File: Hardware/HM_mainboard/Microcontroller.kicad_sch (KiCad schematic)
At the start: 13 parts, among them J7 USB_C_Receptacle_USB2.0, U5 ESP32-S3-WROOM-1, Y1 32.768 kHz

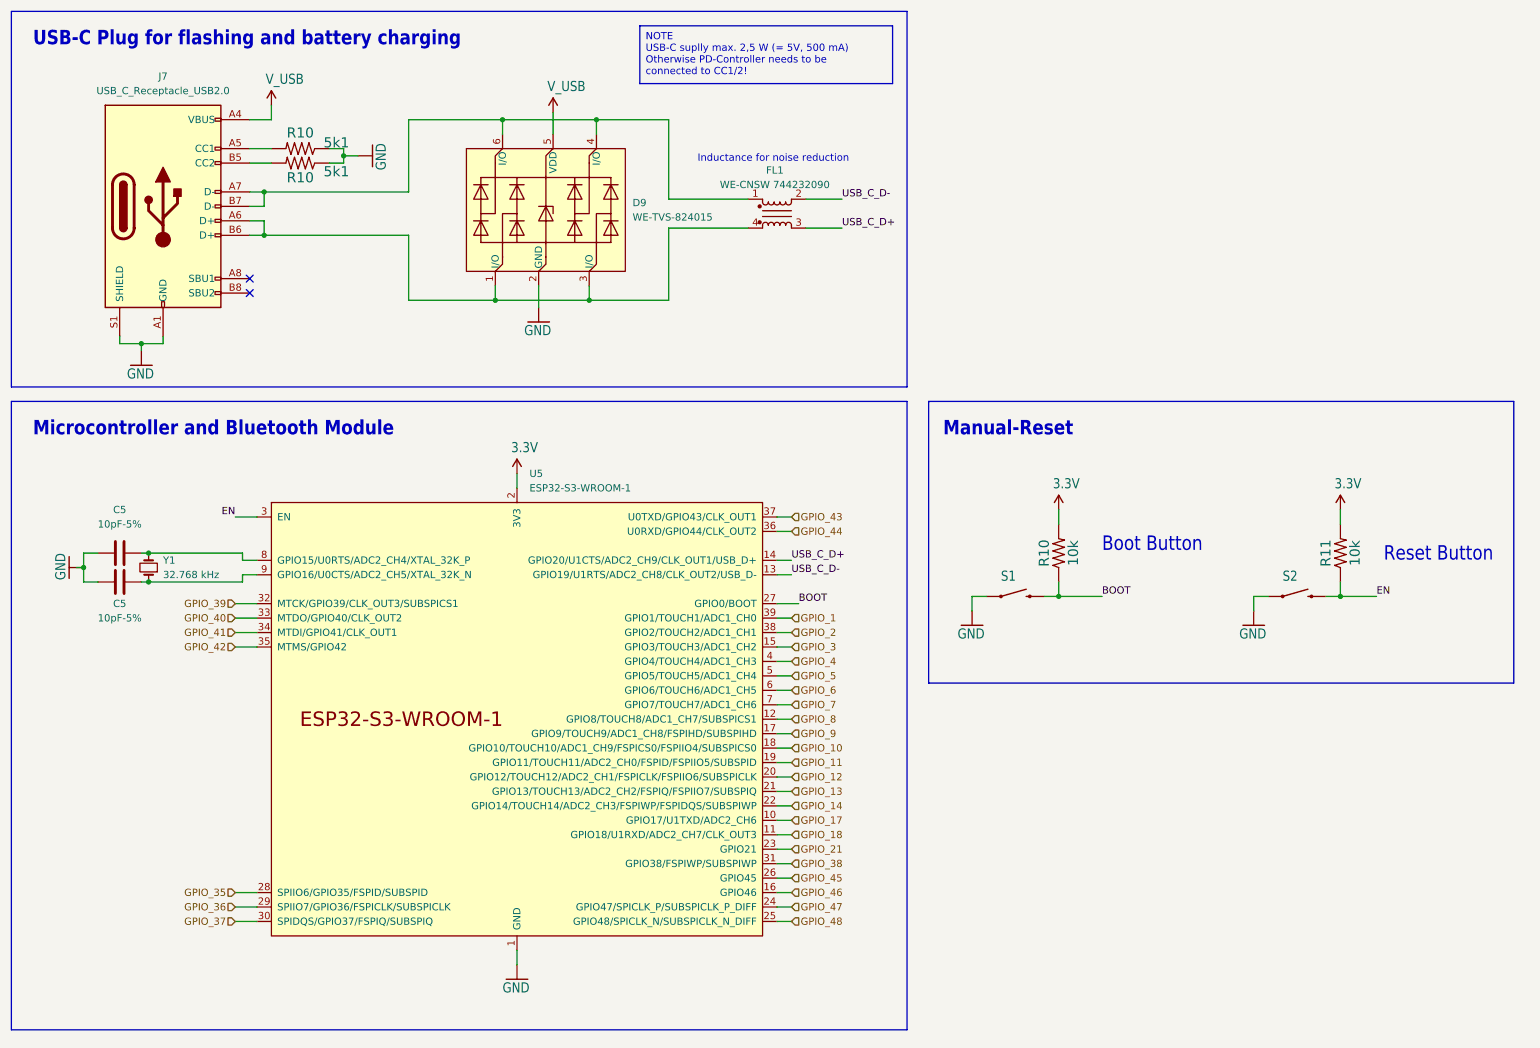
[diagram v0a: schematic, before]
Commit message: Updated components of power supply unit
- Replaced PMOSFET
- Replaced LDO
- Replaced battery charger
- Replaced caps and resistors
- Replaced battery connector
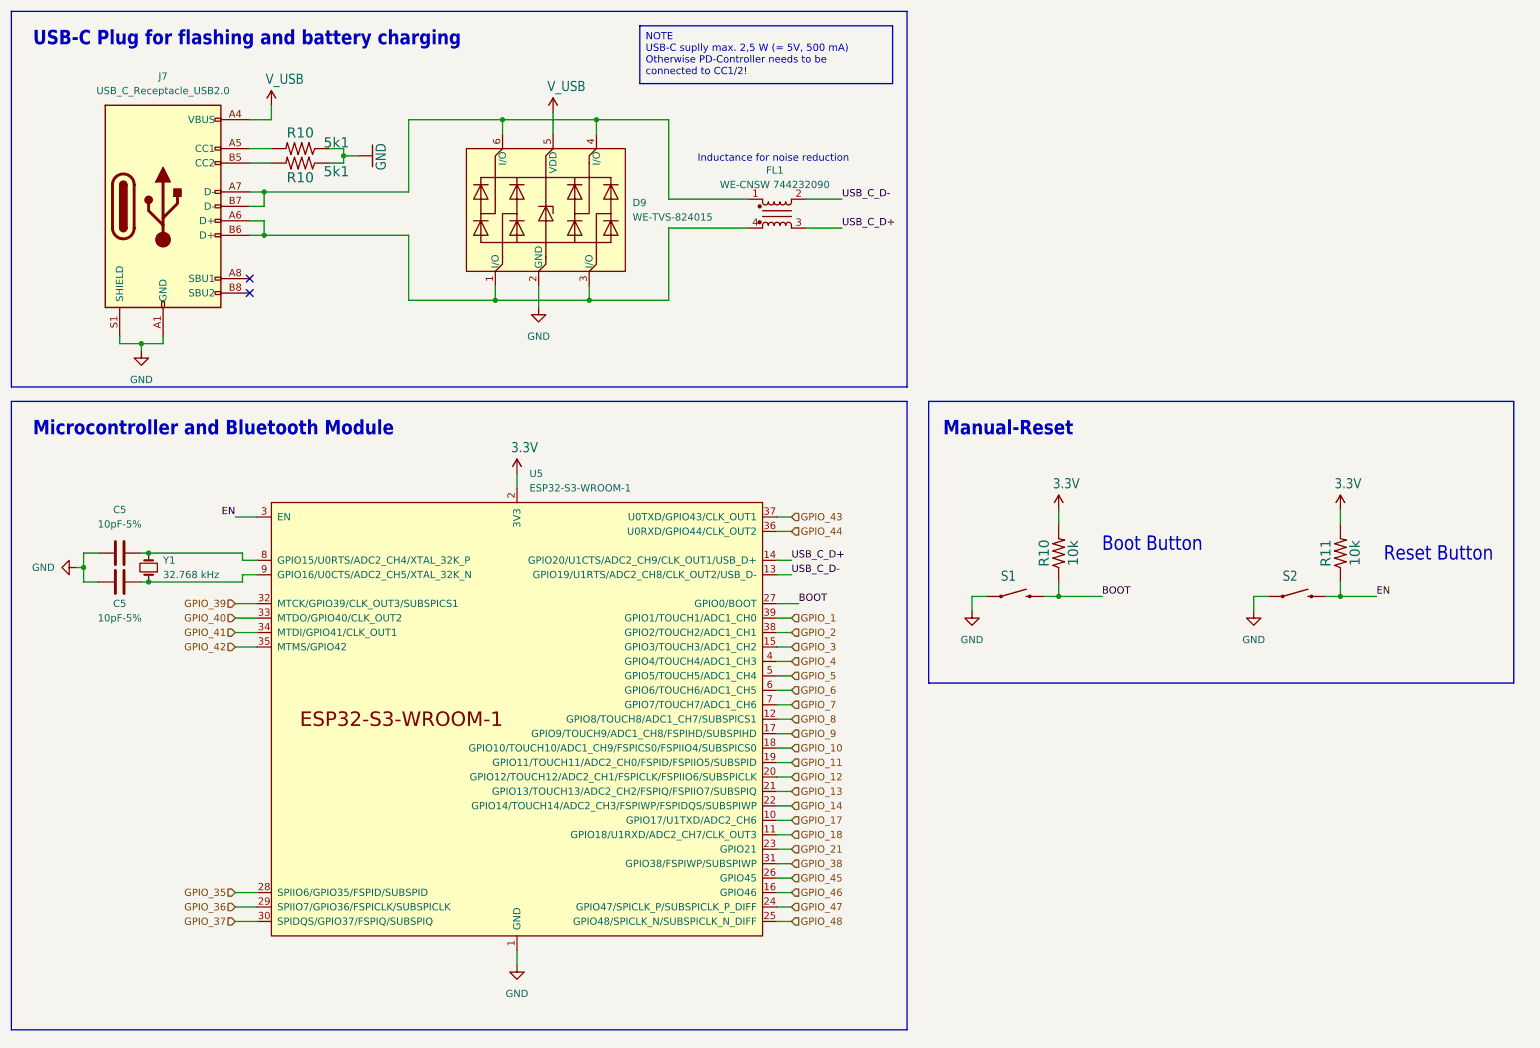
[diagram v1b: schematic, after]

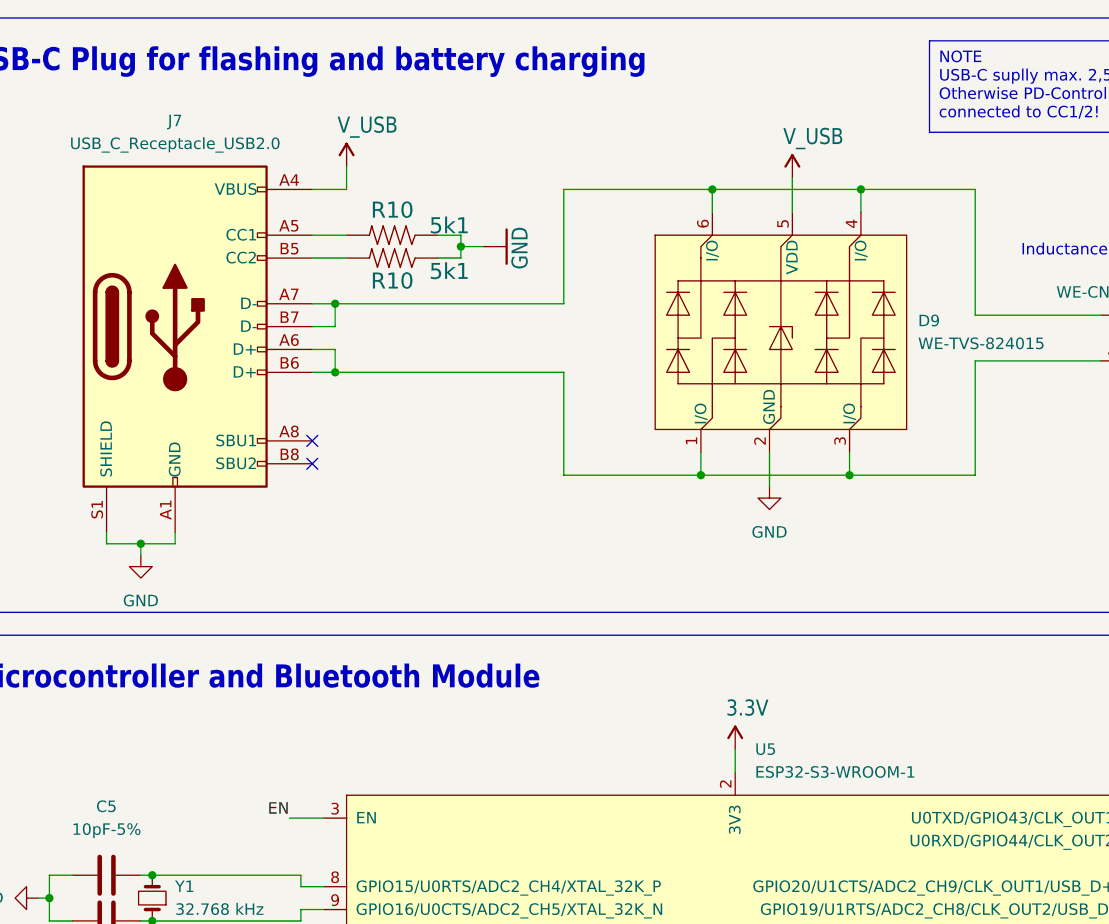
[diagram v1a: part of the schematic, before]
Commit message: Updated port connectors of microcontroller
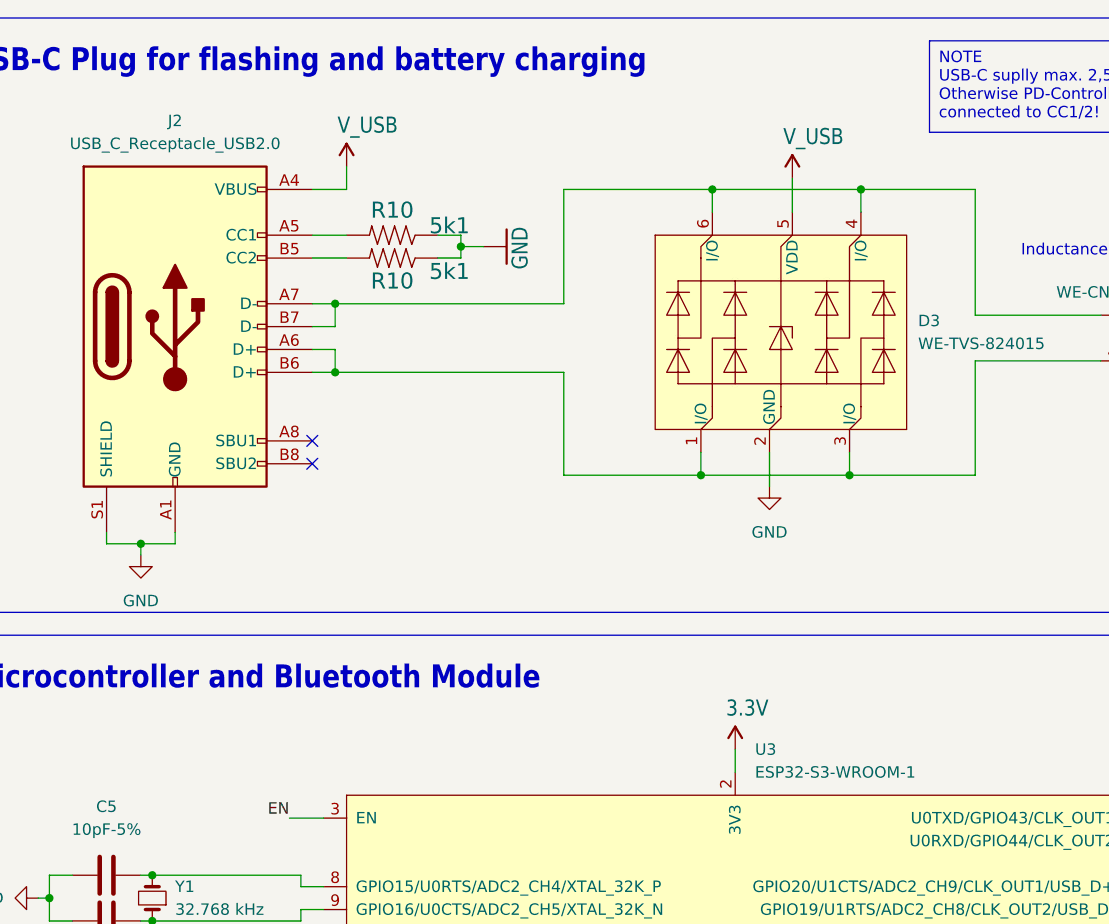
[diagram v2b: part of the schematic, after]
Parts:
- renumbered D9 to D3, J7 to J2, U5 to U3
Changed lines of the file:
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@@
         )
         (path "/54a6df43-5475-46a2-9916-8b0260700d4c/8a725ce3-408a-4762-9df2-b56094186e56"
-          (reference "#PWR019") (unit 1)
+          (reference "#PWR013") (unit 1)
         )
         (path "/54a6df43-5475-46a2-9916-8b0260700d4c/9043a365-e24a-41b8-9f6d-decb4da0da6a"
@@
         )
         (path "/54a6df43-5475-46a2-9916-8b0260700d4c/8a725ce3-408a-4762-9df2-b56094186e56"
-          (reference "#SUPPLY015") (unit 1)
+          (reference "#SUPPLY09") (unit 1)
         )
       )
@@
         )
         (path "/54a6df43-5475-46a2-9916-8b0260700d4c/8a725ce3-408a-4762-9df2-b56094186e56"
-          (reference "#PWR017") (unit 1)
+          (reference "#PWR014") (unit 1)
         )
         (path "/54a6df43-5475-46a2-9916-8b0260700d4c/9043a365-e24a-41b8-9f6d-decb4da0da6a"
@@
   (symbol (lib_id "Connector:USB_C_Receptacle_USB2.0") (at 43.18 49.53 0) (unit 1)
     (in_bom yes) (on_board yes) (dnp no) (fields_autoplaced)
-    (property "Reference" "J7" (at 43.18 26.67 0)
+    (property "Reference" "J2" (at 43.18 26.67 0)
       (effects (font (size 1.27 1.27)))
     )
@@
       (project "HM_mainboard"
         (path "/54a6df43-5475-46a2-9916-8b0260700d4c/8a725ce3-408a-4762-9df2-b56094186e56"
-          (reference "J7") (unit 1)
+          (reference "J2") (unit 1)
         )
       )
@@
         )
         (path "/54a6df43-5475-46a2-9916-8b0260700d4c/8a725ce3-408a-4762-9df2-b56094186e56"
-          (reference "#PWR016") (unit 1)
+          (reference "#PWR012") (unit 1)
         )
         (path "/54a6df43-5475-46a2-9916-8b0260700d4c/9043a365-e24a-41b8-9f6d-decb4da0da6a"
@@
         )
         (path "/54a6df43-5475-46a2-9916-8b0260700d4c/8a725ce3-408a-4762-9df2-b56094186e56"
-          (reference "R15") (unit 1)
+          (reference "R5") (unit 1)
         )
       )
@@
         )
         (path "/54a6df43-5475-46a2-9916-8b0260700d4c/8a725ce3-408a-4762-9df2-b56094186e56"
-          (reference "#GND025") (unit 1)
+          (reference "#GND01") (unit 1)
         )
       )
@@
         )
         (path "/54a6df43-5475-46a2-9916-8b0260700d4c/8a725ce3-408a-4762-9df2-b56094186e56"
-          (reference "#PWR020") (unit 1)
+          (reference "#PWR015") (unit 1)
         )
         (path "/54a6df43-5475-46a2-9916-8b0260700d4c/9043a365-e24a-41b8-9f6d-decb4da0da6a"
@@
   (symbol (lib_id "usePAT:WE-TVS-824015") (at 110.49 50.8 0) (unit 1)
     (in_bom yes) (on_board yes) (dnp no) (fields_autoplaced)
-    (property "Reference" "D9" (at 125.73 48.8949 0)
+    (property "Reference" "D3" (at 125.73 48.8949 0)
       (effects (font (size 1.27 1.27)) (justify left))
     )
@@
       (project "HM_mainboard"
         (path "/54a6df43-5475-46a2-9916-8b0260700d4c/8a725ce3-408a-4762-9df2-b56094186e56"
-          (reference "D9") (unit 1)
+          (reference "D3") (unit 1)
         )
       )
@@
         )
         (path "/54a6df43-5475-46a2-9916-8b0260700d4c/8a725ce3-408a-4762-9df2-b56094186e56"
-          (reference "#SUPPLY016") (unit 1)
+          (reference "#SUPPLY010") (unit 1)
         )
       )
@@
         )
         (path "/54a6df43-5475-46a2-9916-8b0260700d4c/8a725ce3-408a-4762-9df2-b56094186e56"
-          (reference "#SUPPLY07") (unit 1)
+          (reference "#SUPPLY08") (unit 1)
         )
       )
@@
         )
         (path "/54a6df43-5475-46a2-9916-8b0260700d4c/8a725ce3-408a-4762-9df2-b56094186e56"
-          (reference "#PWR021") (unit 1)
+          (reference "#PWR016") (unit 1)
         )
         (path "/54a6df43-5475-46a2-9916-8b0260700d4c/9043a365-e24a-41b8-9f6d-decb4da0da6a"
@@
   (symbol (lib_id "Espressif:ESP32-S3-WROOM-1") (at 105.41 139.7 0) (unit 1)
     (in_bom yes) (on_board yes) (dnp no) (fields_autoplaced)
-    (property "Reference" "U5" (at 107.6041 96.52 0)
+    (property "Reference" "U3" (at 107.6041 96.52 0)
       (effects (font (size 1.27 1.27)) (justify left))
     )
@@
       (project "HM_mainboard"
         (path "/54a6df43-5475-46a2-9916-8b0260700d4c/8a725ce3-408a-4762-9df2-b56094186e56"
-          (reference "U5") (unit 1)
+          (reference "U3") (unit 1)
         )
       )
@@
         )
         (path "/54a6df43-5475-46a2-9916-8b0260700d4c/8a725ce3-408a-4762-9df2-b56094186e56"
-          (reference "R10") (unit 1)
+          (reference "R8") (unit 1)
         )
       )
@@
         )
         (path "/54a6df43-5475-46a2-9916-8b0260700d4c/8a725ce3-408a-4762-9df2-b56094186e56"
-          (reference "C8") (unit 1)
+          (reference "C6") (unit 1)
         )
       )
@@
         )
         (path "/54a6df43-5475-46a2-9916-8b0260700d4c/8a725ce3-408a-4762-9df2-b56094186e56"
-          (reference "#PWR018") (unit 1)
+          (reference "#PWR011") (unit 1)
         )
         (path "/54a6df43-5475-46a2-9916-8b0260700d4c/9043a365-e24a-41b8-9f6d-decb4da0da6a"
@@
         )
         (path "/54a6df43-5475-46a2-9916-8b0260700d4c/8a725ce3-408a-4762-9df2-b56094186e56"
-          (reference "C7") (unit 1)
+          (reference "C5") (unit 1)
         )
       )
@@
         )
         (path "/54a6df43-5475-46a2-9916-8b0260700d4c/8a725ce3-408a-4762-9df2-b56094186e56"
-          (reference "R16") (unit 1)
+          (reference "R6") (unit 1)
         )
       )
@@
         )
         (path "/54a6df43-5475-46a2-9916-8b0260700d4c/8a725ce3-408a-4762-9df2-b56094186e56"
-          (reference "#SUPPLY09") (unit 1)
+          (reference "#SUPPLY012") (unit 1)
         )
       )
@@
         )
         (path "/54a6df43-5475-46a2-9916-8b0260700d4c/8a725ce3-408a-4762-9df2-b56094186e56"
-          (reference "#SUPPLY08") (unit 1)
-        )
-      )
+          (reference "#SUPPLY011") (unit 1)
+        )
+      )
